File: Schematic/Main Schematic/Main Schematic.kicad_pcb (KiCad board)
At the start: 2 copper layers, 100 x 100 mm, 48 parts, among them IC1 DW01A-G, IC2 LM75AD,118, J1 Conn_01x24_Socket, J10 Conn_01x08_Pin, J3 Conn_01x24_Socket, J4 Conn_01x02_Male, J5 Conn_01x02_Male, J6 USB_B_Micro, J7 Conn_01x02_Pin, J8 Conn_01x24_Pin, J9 Conn_01x24_Pin, Q1 FS8205A, SW1 SW_Push, U1 HT75xx-1-SOT89, U2 MCP73831-2-OT, U3 CH340C, U4 M24C16-RMN6TP

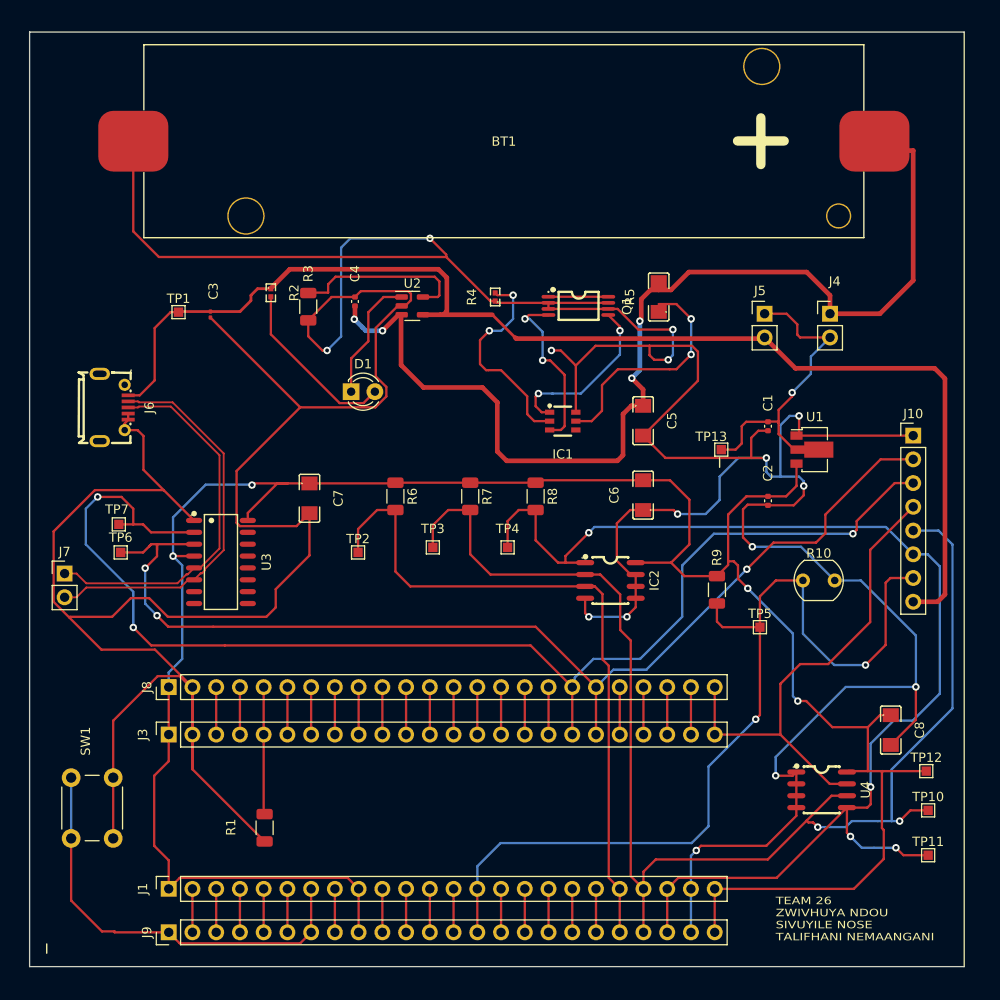
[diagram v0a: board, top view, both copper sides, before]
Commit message: Added the gnd filling zone, moved decoupling caps close to the IC, ensured no tracks are under and IC
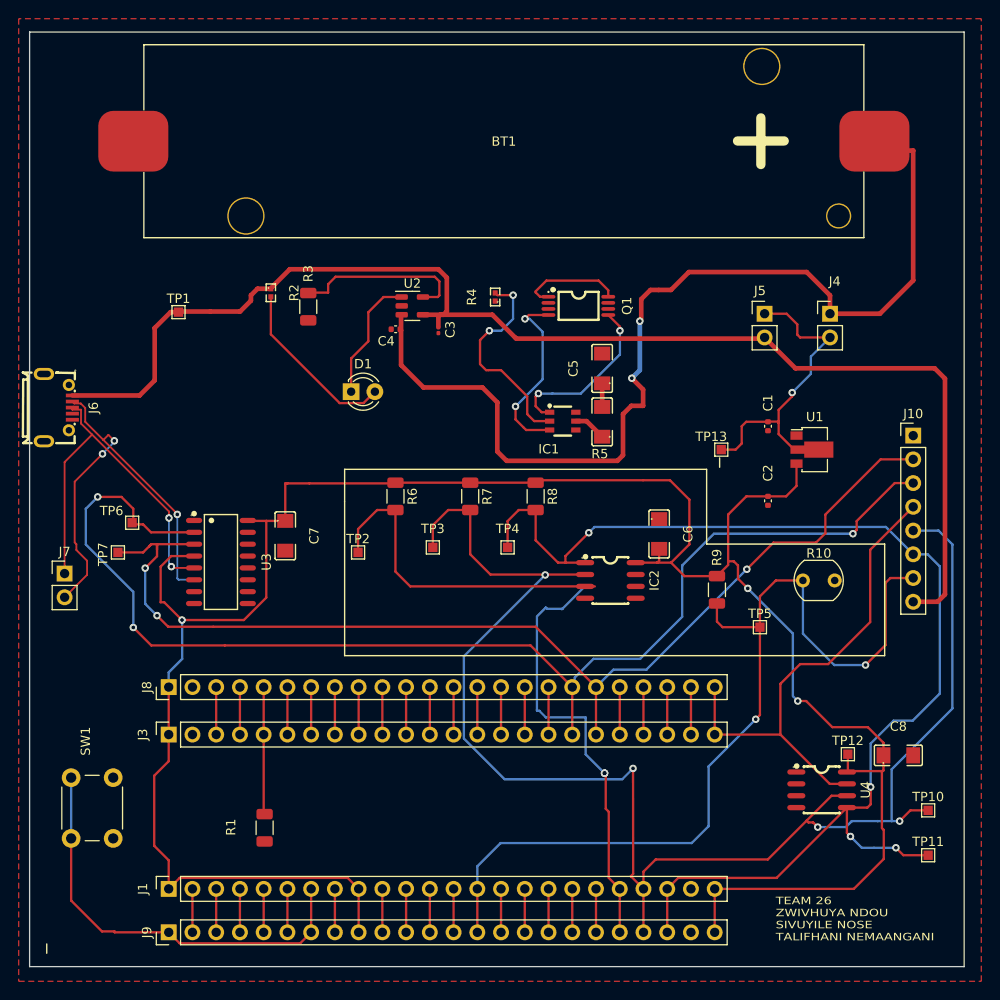
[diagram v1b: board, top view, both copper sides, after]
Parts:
- moved C3 24.5 mm to (144.9, 70.3)
- moved R5 14.7 mm to (162.4, 80.1)
- moved TP12 8.58 mm to (188.7, 115.7)
- moved C5 7.11 mm to (162.4, 74.4), turned to 90 degrees
- moved J6 5.97 mm to (104.2, 78.6)
- moved C4 5.27 mm to (140.3, 70.2), turned to 180 degrees
- moved C7 4.78 mm to (128.5, 92.3)
- moved C6 4.49 mm to (168.5, 92.1), turned to -90 degrees
- moved TP6 3.41 mm to (112.1, 90.9)
- moved TP7 3.00 mm to (110.6, 94.1), turned to 90 degrees
- moved C8 2.83 mm to (194.1, 115.8), turned to 0 degrees
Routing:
- net GND: track 545.1 -> 0.00 mm, vias 15 -> 0
- net Net-(IC1-VCC): track 24.8 -> 3.51 mm, vias 2 -> 0
- net /SCL: track 145.8 -> 163.7 mm, vias 2 -> 4
- net /OS: track 74.0 -> 82.6 mm, vias 0 -> 2
- net /5V: track 133.8 -> 141.2 mm
- net /USB D-: track 42.1 -> 47.9 mm, vias 0 -> 3
- net /Power Unit/V1: track 117.0 -> 112.1 mm, vias 4 -> 2
- net /Power Unit/D12: track 6.40 -> 11.0 mm
- net /TXD: track 135.4 -> 133.9 mm
- net /Power Unit/OC: track 18.5 -> 19.9 mm
- net /USB D+: track 40.5 -> 41.6 mm, vias 0 -> 2
- net /3.3V: track 246.2 -> 246.5 mm, vias 4 -> 3
- added copper zone on F.Cu, net GND

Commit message: Edited the ocb nets for uart
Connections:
- U3 pad 2: /RXD -> /TXD
- U3 pad 3: /TXD -> /RXD

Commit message: Updated the pcb
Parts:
- moved J1 1.13 mm to (116.0, 129.0)
- moved J9 1.03 mm to (116.1, 133.7)
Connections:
- J10 pad 2: /RXD -> /TXD
- J10 pad 3: /TXD -> /RXD
- J3 pad 18: /TXD -> /RXD
- J3 pad 19: /RXD -> /TXD
- J8 pad 18: /TXD -> /RXD
- J8 pad 19: /RXD -> /TXD
- TP6 pad 1: /TXD -> /RXD
- TP7 pad 1: /RXD -> /TXD
- U3 pad 2: /TXD -> /RXD
- U3 pad 3: /RXD -> /TXD
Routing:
- net GND: track 0.00 -> 43.7 mm, vias 0 -> 1
- net /TXD: track 133.9 -> 117.6 mm
- net /RXD: track 118.2 -> 133.5 mm
- net /OS: track 82.6 -> 78.6 mm, vias 2 -> 3
- net /Power Unit/V1: track 112.1 -> 114.9 mm
- net /NRST: track 45.9 -> 47.4 mm
- net /3.3V: track 246.5 -> 247.7 mm
- net /SDL: track 131.9 -> 132.6 mm
- net /SCL: track 163.7 -> 163.1 mm

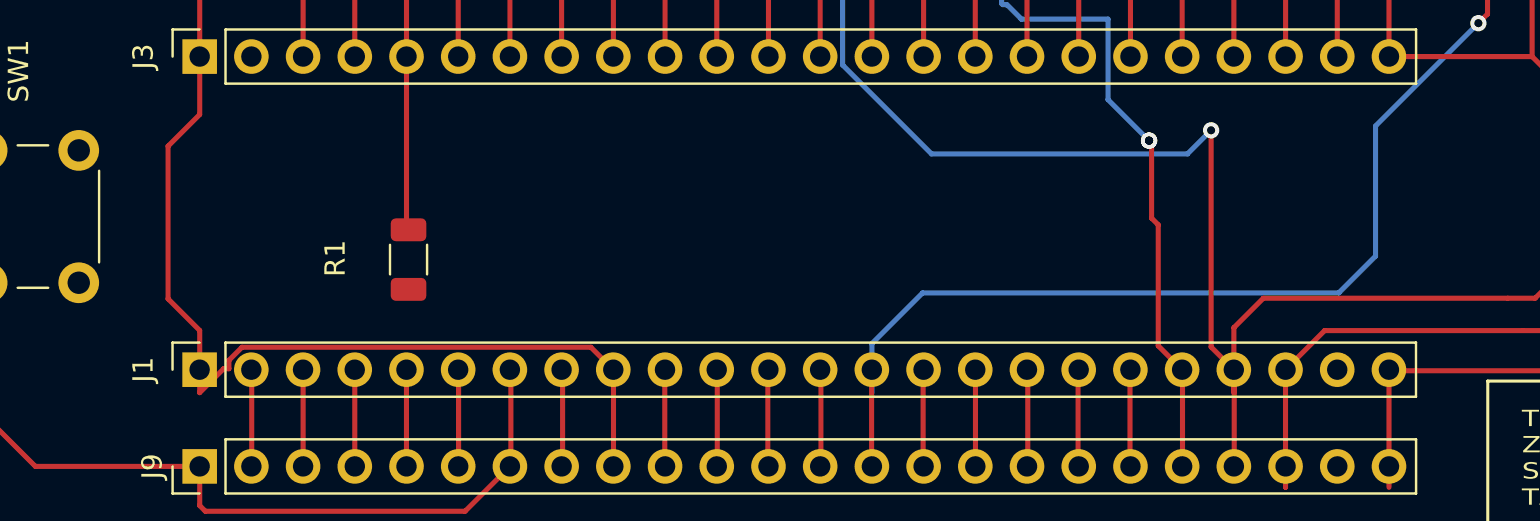
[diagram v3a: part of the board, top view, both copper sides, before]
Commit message: Adjusted the female headers width
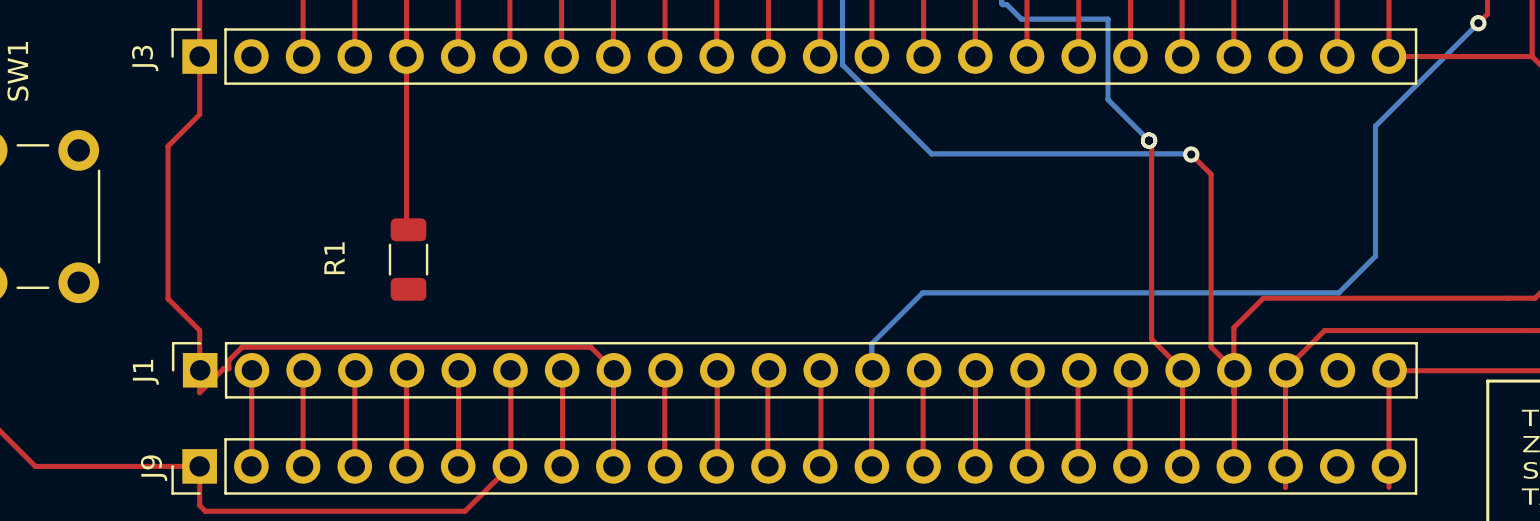
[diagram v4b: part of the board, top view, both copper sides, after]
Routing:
- net /SCL: track 163.1 -> 160.7 mm
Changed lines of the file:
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@@
   )
   (footprint "Connector_PinSocket_2.54mm:PinSocket_1x24_P2.54mm_Vertical" (layer "F.Cu")
-    (at 116.05 128.98 90)
+    (at 116.08 129.01 90)
     (descr "Through hole straight socket strip, 1x24, 2.54mm pitch, single row (from Kicad 4.0.7), script generated")
     (tags "Through hole socket strip THT 1x24 2.54mm single row")
@@
   (segment (start 150.477885 96.474186) (end 160.607781 96.474186) (width 0.25) (layer "F.Cu") (net 13))
   (segment (start 184.311036 122.811036) (end 181.652072 125.47) (width 0.25) (layer "F.Cu") (net 13))
-  (segment (start 165.735 127.865) (end 165.735 117.221) (width 0.25) (layer "F.Cu") (net 13))
   (segment (start 188.617991 120.144188) (end 189.477885 120.144188) (width 0.25) (layer "F.Cu") (net 13))
   (segment (start 184.5 123) (end 184.311036 122.811036) (width 0.25) (layer "F.Cu") (net 13))
@@
   (segment (start 168.3 125.47) (end 166.852886 126.917114) (width 0.25) (layer "F.Cu") (net 13))
   (segment (start 166.87 129.225) (end 166.87 133.875) (width 0.25) (layer "F.Cu") (net 13))
-  (segment (start 166.85 128.98) (end 165.735 127.865) (width 0.25) (layer "F.Cu") (net 13))
   (segment (start 181.652072 125.47) (end 180.3 125.47) (width 0.25) (layer "F.Cu") (net 13))
   (segment (start 188.617991 120.144188) (end 186.977885 120.144188) (width 0.25) (layer "F.Cu") (net 13))
-  (segment (start 165.735 117.221) (end 165.750886 117.205114) (width 0.25) (layer "F.Cu") (net 13))
+  (segment (start 166.85 128.98) (end 165.735 127.865) (width 0.25) (layer "F.Cu") (net 13))
   (segment (start 144.312886 91.209187) (end 145.950386 89.571687) (width 0.25) (layer "F.Cu") (net 13))
   (segment (start 185.5 123.5) (end 185 123) (width 0.25) (layer "F.Cu") (net 13))
   (segment (start 166.852886 126.917114) (end 166.852886 130.109187) (width 0.25) (layer "F.Cu") (net 13))
+  (segment (start 165.735 127.865) (end 165.735 119.385) (width 0.25) (layer "F.Cu") (net 13))
   (segment (start 186.977885 120.144188) (end 184.311036 122.811036) (width 0.25) (layer "F.Cu") (net 13))
   (segment (start 195.412886 121.709187) (end 194.262886 122.859187) (width 0.25) (layer "F.Cu") (net 13))
   (segment (start 148.312886 94.309187) (end 150.477885 96.474186) (width 0.25) (layer "F.Cu") (net 13))
   (segment (start 148.312886 89.571687) (end 148.312886 94.309187) (width 0.25) (layer "F.Cu") (net 13))
+  (segment (start 165.735 119.385) (end 164.76 118.41) (width 0.25) (layer "F.Cu") (net 13))
   (segment (start 144.312886 93.571687) (end 144.312886 91.209187) (width 0.25) (layer "F.Cu") (net 13))
-  (via (at 165.735 117.221) (size 0.8) (drill 0.4) (layers "F.Cu" "B.Cu") (net 13))
+  (via (at 164.76 118.41) (size 0.8) (drill 0.4) (layers "F.Cu" "B.Cu") (net 13))
   (via (at 156.337 96.52) (size 0.8) (drill 0.4) (layers "F.Cu" "B.Cu") (net 13))
   (via (at 185.5 123.5) (size 0.8) (drill 0.4) (layers "F.Cu" "B.Cu") (net 13))
@@
   (segment (start 199.912886 93.259187) (end 198.422886 91.769187) (width 0.25) (layer "B.Cu") (net 13))
   (segment (start 191.912886 122.859187) (end 189.140813 122.859187) (width 0.25) (layer "B.Cu") (net 13))
-  (segment (start 165.735 117.221) (end 164.575 118.381) (width 0.25) (layer "B.Cu") (net 13))
   (segment (start 152.002 118.381) (end 147.634886 114.013886) (width 0.25) (layer "B.Cu") (net 13))
   (segment (start 164.575 118.381) (end 152.002 118.381) (width 0.25) (layer "B.Cu") (net 13))
@@
   (segment (start 189.140813 122.859187) (end 188.5 123.5) (width 0.25) (layer "B.Cu") (net 13))
   (segment (start 193.412886 122.859187) (end 193.412886 117.309187) (width 0.25) (layer "B.Cu") (net 13))
-  (segment (start 163.137886 121.862886) (end 162.814 121.539) (width 0.25) (layer "F.Cu") (net 14))
+  (segment (start 164.31 128.98) (end 162.814 127.484) (width 0.25) (layer "F.Cu") (net 14))
   (segment (start 162.687 117.729) (end 162.56 117.729) (width 0.25) (layer "F.Cu") (net 14))
   (segment (start 156.45 97.744188) (end 141.897887 97.744188) (width 0.25) (layer "F.Cu") (net 14))
+  (segment (start 162.687 117.856) (end 162.687 117.729) (width 0.25) (layer "F.Cu") (net 14))
+  (segment (start 160.607781 97.744188) (end 156.45 97.744188) (width 0.25) (layer "F.Cu") (net 14))
+  (segment (start 164.33 128.965) (end 164.33 133.615) (width 0.25) (layer "F.Cu") (net 14))
   (segment (start 162.814 117.983) (end 162.687 117.856) (width 0.25) (layer "F.Cu") (net 14))
-  (segment (start 160.607781 97.744188) (end 156.45 97.744188) (width 0.25) (layer "F.Cu") (net 14))
-  (segment (start 162.687 117.856) (end 162.687 117.729) (width 0.25) (layer "F.Cu") (net 14))
-  (segment (start 164.33 128.965) (end 164.33 133.615) (width 0.25) (layer "F.Cu") (net 14))
-  (segment (start 162.814 121.539) (end 162.814 117.983) (width 0.25) (layer "F.Cu") (net 14))
   (segment (start 161.647887 97.744188) (end 160.607781 97.744188) (width 0.25) (layer "F.Cu") (net 14))
   (segment (start 136.312886 91.609187) (end 138.350386 89.571687) (width 0.25) (layer "F.Cu") (net 14))
   (segment (start 141.897887 97.744188) (end 140.312886 96.159187) (width 0.25) (layer "F.Cu") (net 14))
   (segment (start 162.56 117.729) (end 162.56 117.729) (width 0.25) (layer "F.Cu") (net 14))
-  (segment (start 163.137886 127.807886) (end 163.137886 121.862886) (width 0.25) (layer "F.Cu") (net 14))
+  (segment (start 162.814 127.484) (end 162.814 117.983) (width 0.25) (layer "F.Cu") (net 14))
   (segment (start 138.350386 89.571687) (end 140.312886 89.571687) (width 0.25) (layer "F.Cu") (net 14))
   (segment (start 136.312886 94.109187) (end 136.312886 91.609187) (width 0.25) (layer "F.Cu") (net 14))
-  (segment (start 164.31 128.98) (end 163.137886 127.807886) (width 0.25) (layer "F.Cu") (net 14))
   (segment (start 156.45 99.95) (end 156.45 97.744188) (width 0.25) (layer "F.Cu") (net 14))
   (segment (start 140.312886 96.159187) (end 140.312886 89.571687) (width 0.25) (layer "F.Cu") (net 14))

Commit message: Update
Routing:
- net /USB D-: track 47.5 -> 47.6 mm, vias 3 -> 4
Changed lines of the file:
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@@
   (segment (start 116.332 95.504) (end 116.332 95.631) (width 0.2) (layer "B.Cu") (net 53))
   (segment (start 116.967 89.9788) (end 116.967 90.043) (width 0.2) (layer "F.Cu") (net 54))
+  (segment (start 117.449185 97.039185) (end 118.767902 97.039185) (width 0.2) (layer "F.Cu") (net 54))
   (segment (start 105.952166 78.173006) (end 106.642561 78.173006) (width 0.2) (layer "F.Cu") (net 54))
   (segment (start 109.601 81.534) (end 109.0616 82.0734) (width 0.2) (layer "F.Cu") (net 54))
@@
   (segment (start 110.236 82.169) (end 109.601 81.534) (width 0.2) (layer "F.Cu") (net 54))
   (segment (start 105.989886 86.542114) (end 108.966 83.566) (width 0.2) (layer "F.Cu") (net 54))
+  (segment (start 116.96 96.55) (end 117.449185 97.039185) (width 0.2) (layer "F.Cu") (net 54))
   (segment (start 117.0312 90.043) (end 116.9991 90.0109) (width 0.2) (layer "F.Cu") (net 54))
   (segment (start 104.912886 98.909187) (end 107.315 96.507073) (width 0.2) (layer "F.Cu") (net 54))
   (via (at 110.236 82.169) (size 0.8) (drill 0.4) (layers "F.Cu" "B.Cu") (net 54))
   (via (at 108.966 83.566) (size 0.8) (drill 0.4) (layers "F.Cu" "B.Cu") (net 54))
+  (via (at 116.96 96.55) (size 0.8) (drill 0.4) (layers "F.Cu" "B.Cu") (net 54))
   (via (at 116.967 90.043) (size 0.8) (drill 0.4) (layers "F.Cu" "B.Cu") (net 54))
+  (segment (start 116.967 90.043) (end 116.96 96.55) (width 0.2) (layer "B.Cu") (net 54))
   (segment (start 110.236 82.296) (end 110.236 82.169) (width 0.2) (layer "B.Cu") (net 54))
-  (segment (start 117.5 97.05) (end 118.75 97.05) (width 0.2) (layer "B.Cu") (net 54))
   (segment (start 108.966 83.566) (end 110.236 82.296) (width 0.2) (layer "B.Cu") (net 54))
-  (segment (start 116.967 96.517) (end 117.5 97.05) (width 0.2) (layer "B.Cu") (net 54))
-  (segment (start 116.967 90.043) (end 116.967 96.517) (width 0.2) (layer "B.Cu") (net 54))
+  (segment (start 116.96 96.55) (end 116.967 96.527) (width 0.2) (layer "B.Cu") (net 54))
   (segment (start 155.780914 66.753914) (end 156.682531 66.753914) (width 0.25) (layer "F.Cu") (net 55))
   (segment (start 163.083343 66.055343) (end 162.052 65.024) (width 0.25) (layer "F.Cu") (net 55))

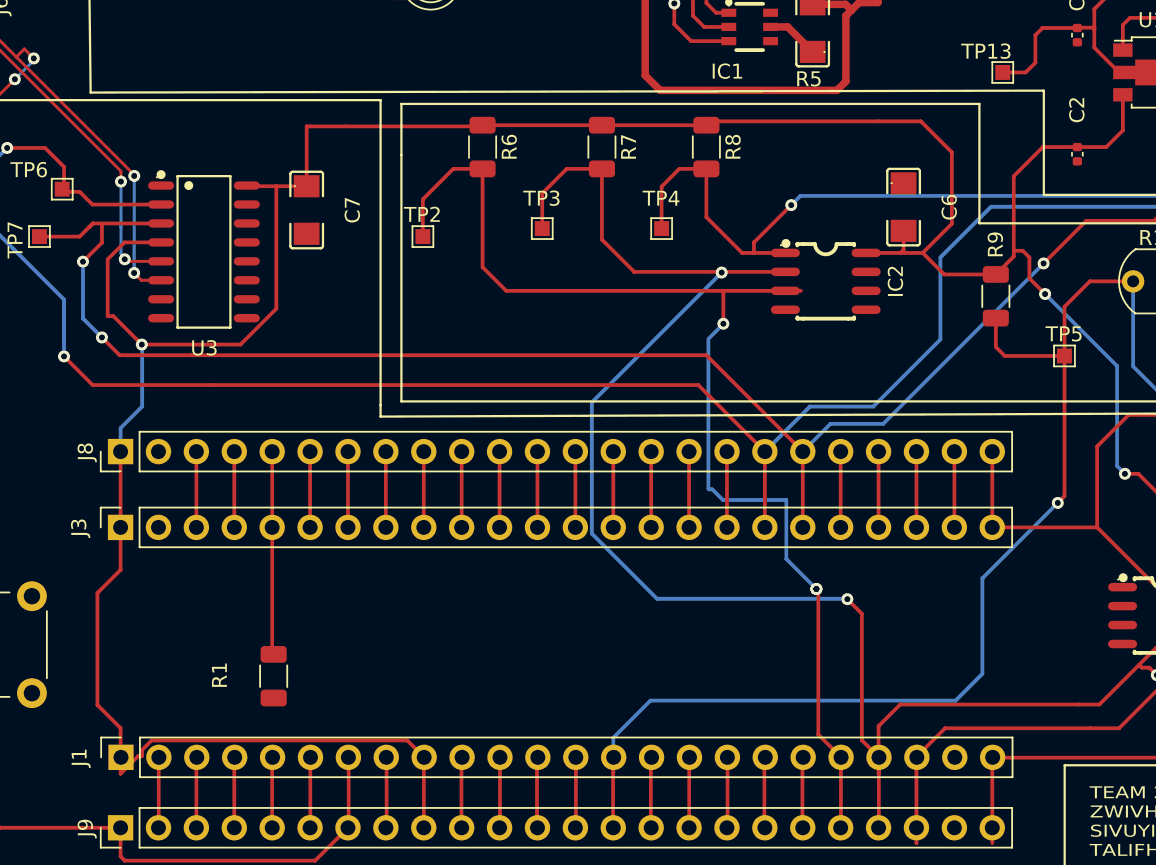
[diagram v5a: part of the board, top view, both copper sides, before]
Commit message: Added conn for sensor
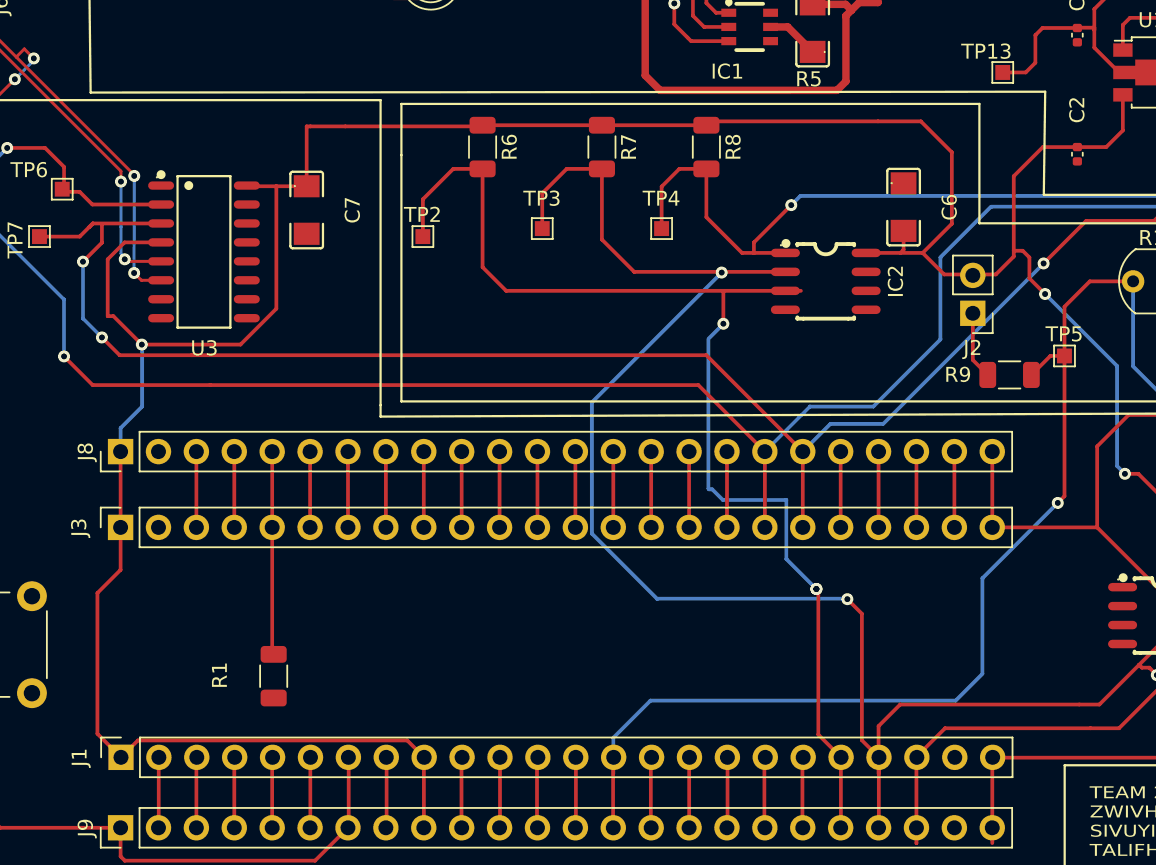
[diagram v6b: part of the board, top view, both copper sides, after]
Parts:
- added J2: Conn_01x02_Pin, Connector_PinHeader_2.54mm:PinHeader_1x02_P2.54mm_Vertical, F.Cu at (173.2, 99.2)
- moved R9 5.35 mm to (175.6, 103.4), turned to 0 degrees
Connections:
- J10 pad 2: /TXD -> (no net)
- J3 pad 19: /TXD -> (no net)
- J8 pad 19: /TXD -> (no net)
- R9 pad 1: /3.3V -> (no net)
- TP7 pad 1: /TXD -> (no net)
- U3 pad 3: /TXD -> (no net)
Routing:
- net /TXD: track 117.6 -> 122.2 mm
- net /ADC: track 99.4 -> 95.3 mm
- net /3.3V: track 247.7 -> 245.9 mm
